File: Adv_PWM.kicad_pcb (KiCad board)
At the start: 2 copper layers, 37.2 x 29 mm, 15 parts, among them IC1 ATTINY13-P, P1 CONN_01X03, P2 CONN_01X03, SW1 Rotary_Encoder_Switch, U1 LTV-817

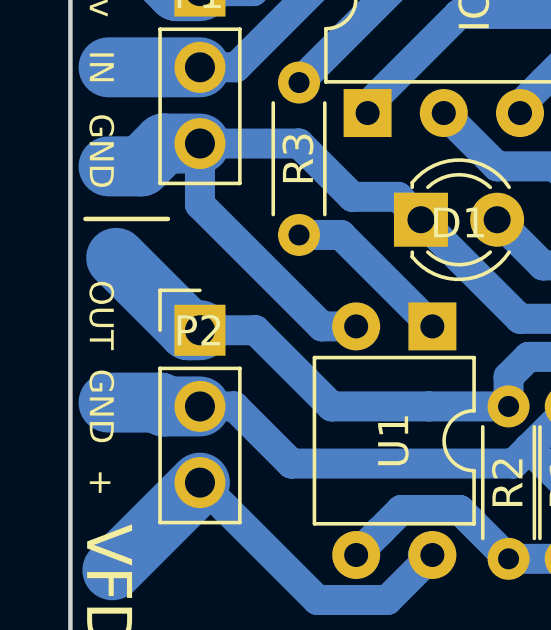
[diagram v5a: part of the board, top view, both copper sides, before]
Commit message: Rename silkscreen label
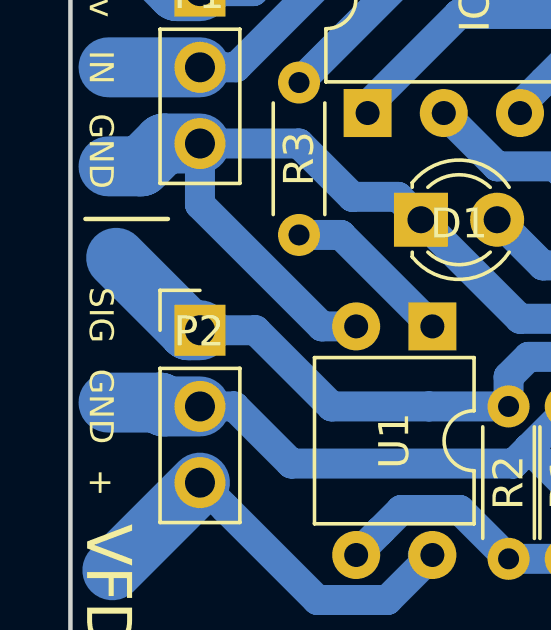
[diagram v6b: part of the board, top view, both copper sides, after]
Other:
- board text added: "SIG"
- board text removed: "OUT"
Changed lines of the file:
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@@
   (gr_line (start 142 74.25) (end 173 74.25) (layer Edge.Cuts) (width 0.15))
   (gr_line (start 179.25 103.25) (end 142 103.25) (layer Edge.Cuts) (width 0.15))
-  (gr_text OUT (at 143.016 92.202 270) (layer F.SilkS)
+  (gr_text SIG (at 143.016 92.202 270) (layer F.SilkS)
     (effects (font (size 0.8 0.8) (thickness 0.2)))
   )
